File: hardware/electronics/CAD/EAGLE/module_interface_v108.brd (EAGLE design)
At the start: 165.1 x 83.4 mm, 42 parts, among them J3 61200621621, U3 SN74HCT32DRD14, U4 SN74HCT32DRD14, U5 ULN2003ADRD0016A_N, U6 ULN2003ADRD0016A_N

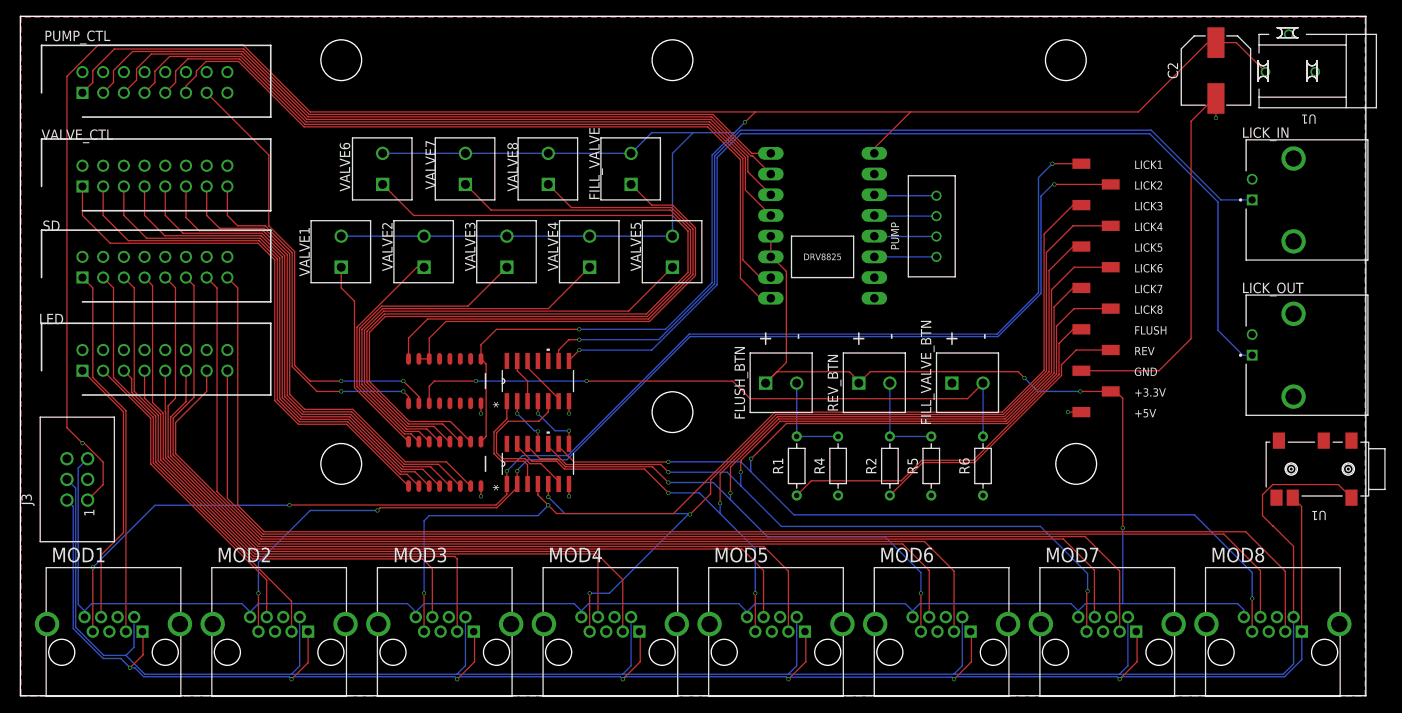
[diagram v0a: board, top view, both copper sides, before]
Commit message: added headers for motor driver
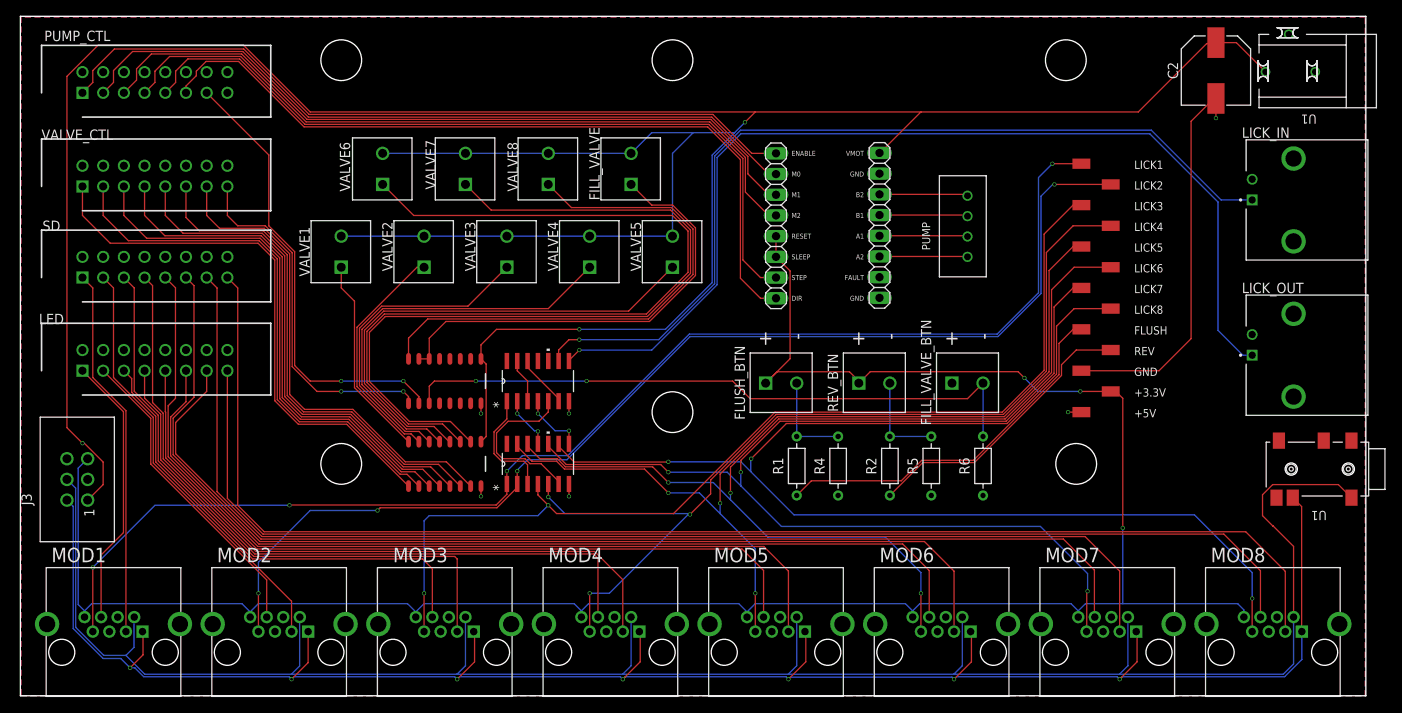
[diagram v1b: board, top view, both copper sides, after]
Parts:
- removed U$1: DRV8825, DRV8825:DRV8825
- added JP1, JP2: PINHD-1X8, Connector:1X08
- moved PUMP 3.81 mm to (109.9, 68.6)
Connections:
- removed net N$18: PUMP_CTL.1, U$1.1
- removed net N$19: PUMP_CTL.3, U$1.2
- removed net N$20: PUMP_CTL.5, U$1.3
- removed net N$21: PUMP_CTL.7, U$1.4
- removed net N$22: PUMP_CTL.9, U$1.7
- removed net N$23: PUMP_CTL.11, U$1.8
- removed net N$30: PUMP.4, U$1.11
- removed net N$31: PUMP.3, U$1.12
- removed net N$32: PUMP.2, U$1.13
- removed net N$33: PUMP.1, U$1.14
- new net A1: JP2.5, PUMP.2
- new net A2: JP2.6, PUMP.1
- new net B1: JP2.4, PUMP.3
- new net B2: JP2.3, PUMP.4
- new net DIR: JP1.8, PUMP_CTL.11
- new net ENABLE: JP1.1, PUMP_CTL.1
- new net M0: JP1.2, PUMP_CTL.3
- new net M1: JP1.3, PUMP_CTL.5
- new net M2: JP1.4, PUMP_CTL.7
- new net STEP: JP1.7, PUMP_CTL.9
- net +12V: now also JP2.1; no longer U$1.9
- net +3.3V: now also JP1.5, JP1.6; no longer U$1.5, U$1.6
- net GND: now also JP2.2, JP2.8; no longer U$1.10, U$1.16
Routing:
- net STEP: track 0.00 -> 95.9 mm
- net DIR: track 0.00 -> 95.4 mm
- net N$22: track 95.2 -> 0.00 mm
- net N$23: track 94.7 -> 0.00 mm
- net ENABLE: track 0.00 -> 93.5 mm
- net N$18: track 92.8 -> 0.00 mm
- net M0: track 0.00 -> 91.7 mm
- net M1: track 0.00 -> 91.2 mm
- net N$19: track 91.1 -> 0.00 mm
- net M2: track 0.00 -> 90.7 mm
- net N$20: track 90.4 -> 0.00 mm
- net N$21: track 89.9 -> 0.00 mm
- net B2: track 0.00 -> 10.9 mm
- net B1: track 0.00 -> 10.8 mm
- net A1: track 0.00 -> 10.8 mm
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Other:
- board text added: "A1"
- board text added: "A2"
- board text added: "B1"
- board text added: "B2"
- board text added: "DIR"
- board text added: "ENABLE"
- board text added: "FAULT"
- board text added: "M0"
- board text added: "M1"
- board text added: "M2"
- board text added: "RESET"
- board text added: "SLEEP"
- board text added: "STEP"
- board text added: "VMOT"
